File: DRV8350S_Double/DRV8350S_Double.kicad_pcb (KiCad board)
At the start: 4 copper layers, 180.5 x 154.9 mm, 248 parts, among them IC1 MCP1501T-33, J1 USB_OTG, J10 Screw_Terminal_01x01, J11 Screw_Terminal_01x01, J12 Screw_Terminal_01x01, J13 Screw_Terminal_01x01, J14 Screw_Terminal_01x01, J15 Screw_Terminal_01x01, J16 Screw_Terminal_01x01, J17 Screw_Terminal_01x01, J18 Conn_01x08, J2 Conn_02x07_Odd_Even, J3 Conn_01x04, J4 47272-0001, J5 Conn_01x08, J6 Conn_01x08, J7 Conn_01x08, J8 Conn_01x08, J9 47272-0001, Q1 Q_NMOS_GDS, Q10 Q_NMOS_GDS, Q11 Q_NMOS_GDS, Q12 Q_NMOS_GDS, Q2 Q_NMOS_GDS, Q3 Q_NMOS_GDS, Q4 Q_NMOS_GDS, Q5 Q_NMOS_GDS, Q6 Q_NMOS_GDS, Q7 Q_NMOS_GDS, Q8 Q_NMOS_GDS, Q9 Q_NMOS_GDS, SW2 SW_Push, U1 LM5017MR, U10 SN65LVDS31D, U11 LM324DR, U12 LM324DR, U13 ESD122DMXR, U14 SN65LVDS33D, U15 LSF0204PWR, U16 LSF0204PWR, U17 LM324DR, U2 ADUM4160, U3 LM2576HVS-5, U4 LM2576HVS-3.3, U5 ISO1050-CUSTOM-SuperDriver_1.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, U6 STM32H743VITx, U7 DRV8350, U8 DRV8350, U9 SN65LVDS31D, Y1 SIT8008AI-82-33E-22.118400

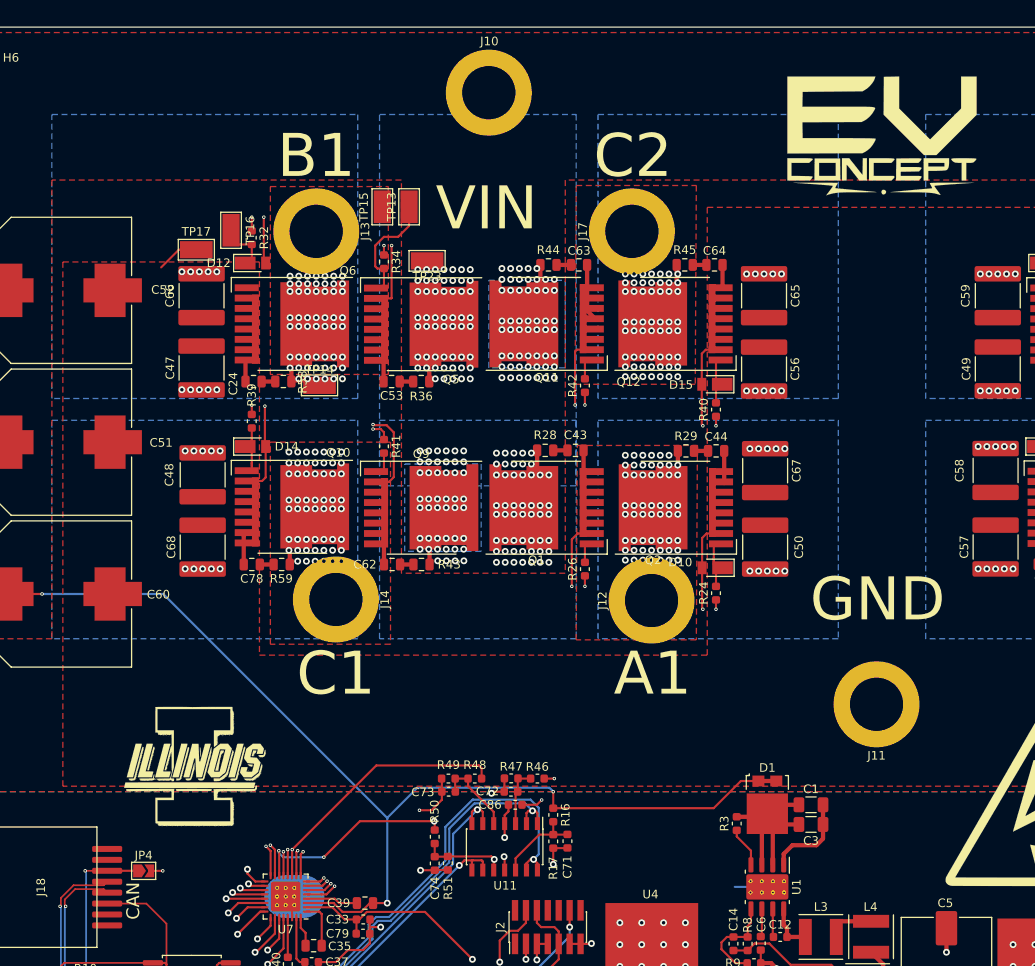
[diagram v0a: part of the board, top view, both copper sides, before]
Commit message: fixed iso_gnd miss
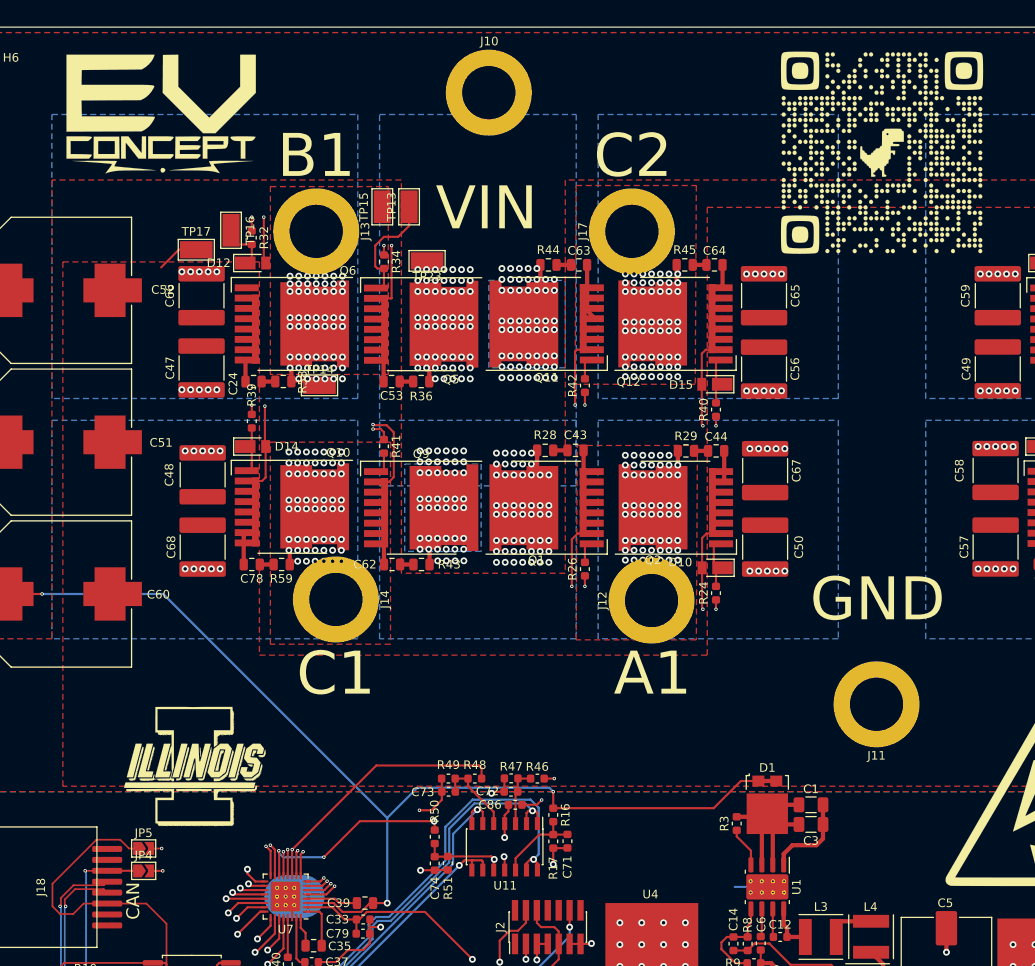
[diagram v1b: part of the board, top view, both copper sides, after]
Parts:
- added JP5: SJ-O, Jumper:SolderJumper-2_P1.3mm_Open_TrianglePad1.0x1.5mm, F.Cu at (56.4, 110.7)
- added NA3: Image, EVCONCEPT:qrcode_github, F.Cu at (142.2, 29.8)
- moved NA2 83.9 mm to (58.4, 25.4)
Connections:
- R41 pad 1: C1 -> GHC1
- U7 pad 13: C1 -> GHC1
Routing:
- net GHC1: track 0.00 -> 61.9 mm, vias 0 -> 3
- net C1: track 167.1 -> 105.2 mm, vias 61 -> 58
- net GND_ISO: track 59.1 -> 81.4 mm
- net GND: track 1005.9 -> 1007.3 mm, vias 116 -> 117

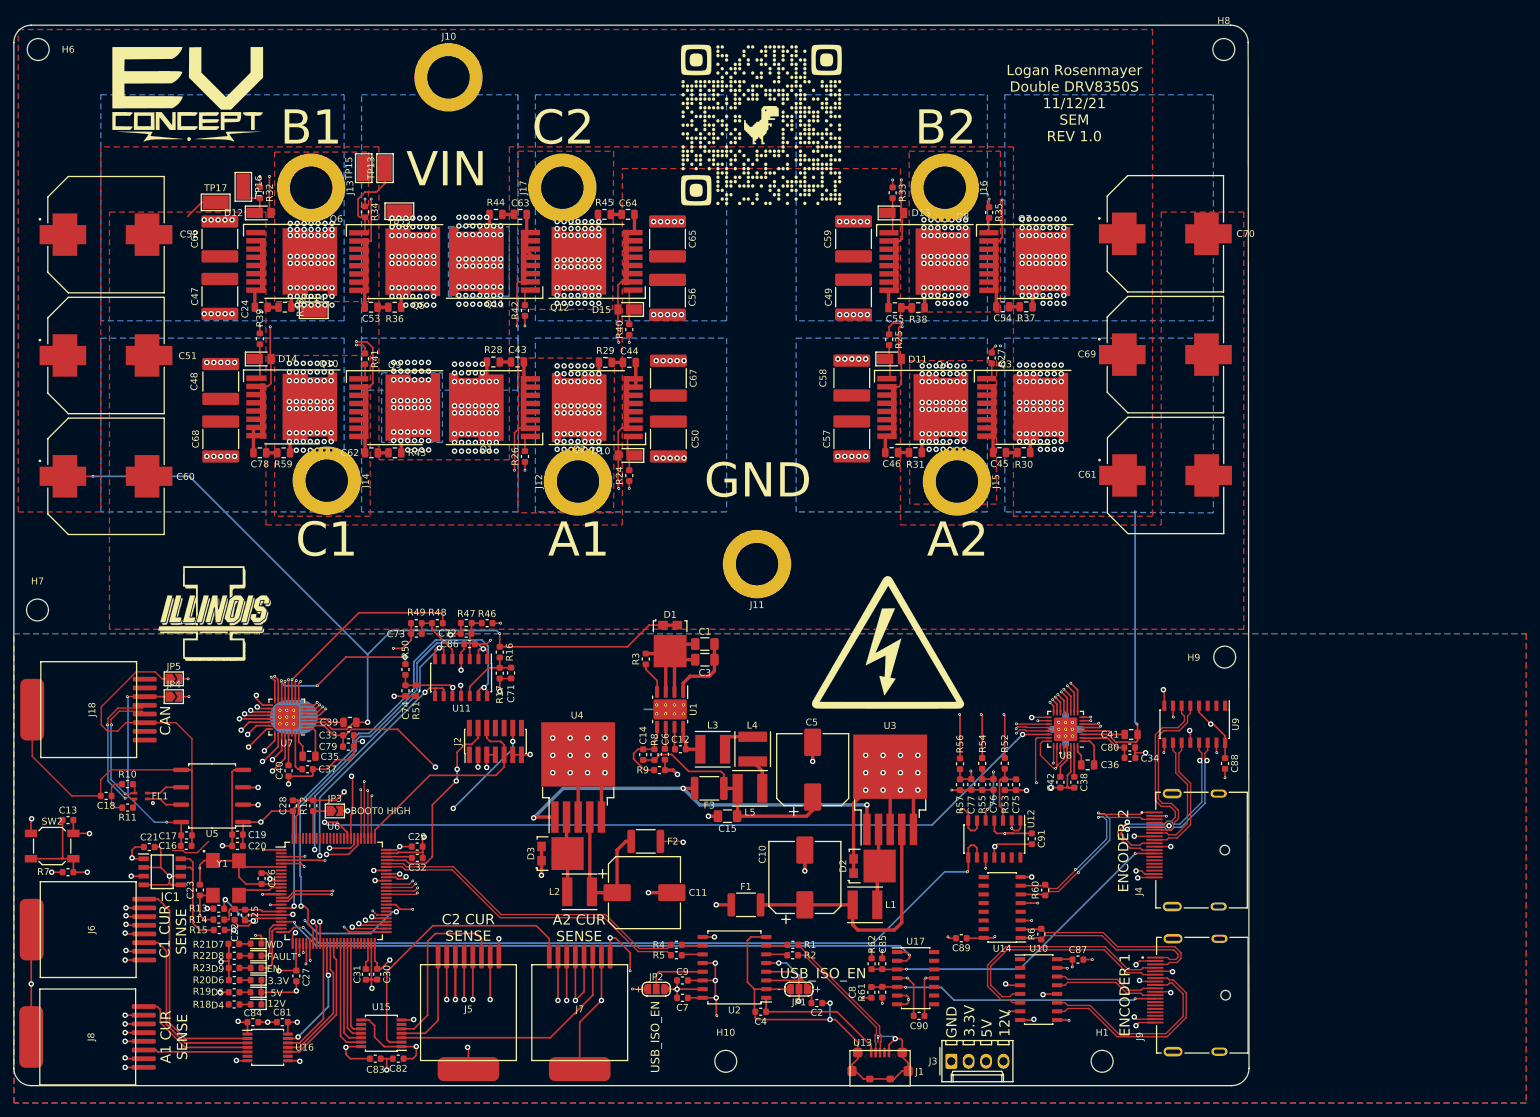
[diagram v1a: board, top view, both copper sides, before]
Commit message: Backing up current design
Fucked up something with STM32 and displayport is dumb
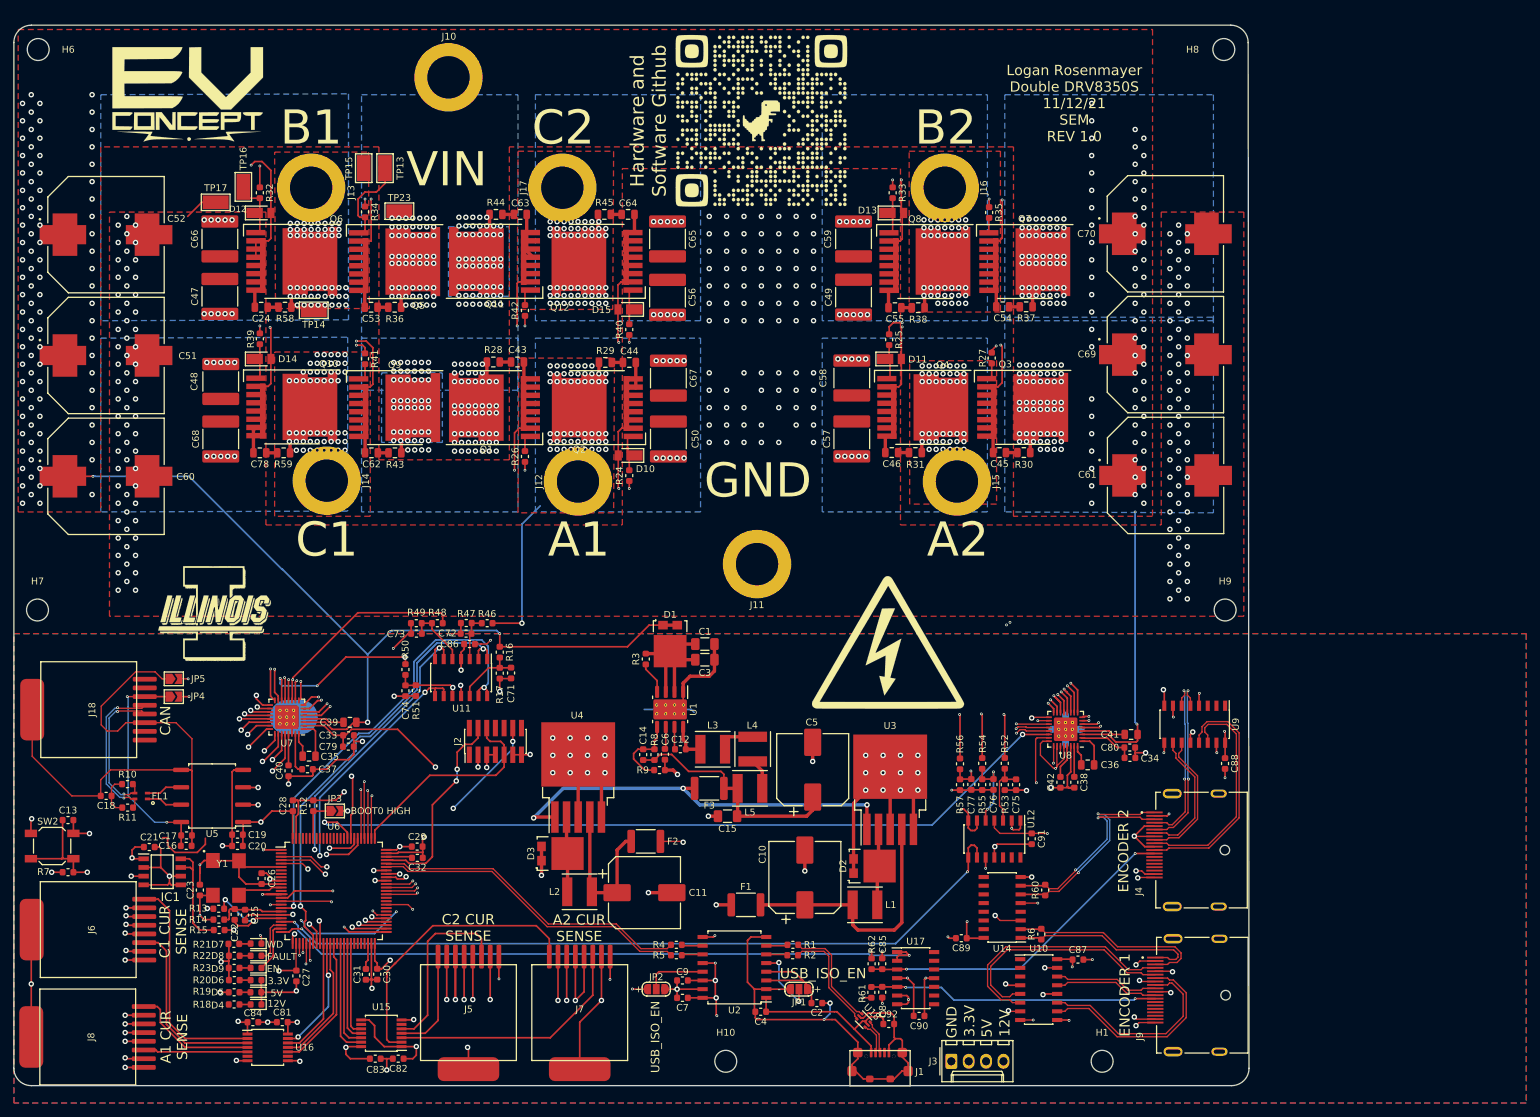
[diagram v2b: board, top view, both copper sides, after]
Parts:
- removed U13: ESD122DMXR, EVCONCEPT:IC_ESD122DMXR
- added C92: 0.1uF, Capacitor_SMD:C_0603_1608Metric, F.Cu at (160.8, 161.2)
- added NA7: Image, EVCONCEPT:qr_code_rick_roll, F.Cu at (142.2, 29.2)
- added U18: USBLC6-2SC6, Package_TO_SOT_SMD:SOT-666, F.Cu at (157.2, 160.7)
- NA3: moved to B.Cu
- moved NA3 128.0 mm to (49.5, 118.1), turned to 180 degrees
- moved H9 6.88 mm to (210.0, 100.7)
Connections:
- net ~Fault1 renamed ~{Fault1}
- net ~Fault2 renamed ~{Fault2}
- J1 pad 2: /UD_Conn_- -> /UD_Conn_preESD_-
- J1 pad 3: /UD_Conn_+ -> /UD_Conn_preESD_+
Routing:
- net GND: track 1007.3 -> 1041.3 mm, vias 117 -> 326
- net GLB1: track 81.6 -> 98.8 mm
- net A2: track 102.8 -> 111.9 mm, vias 58 -> 44
- net +5V: track 74.0 -> 64.9 mm, vias 16 -> 15
- net VBUS1: track 20.4 -> 27.0 mm
- net USBGND: track 65.5 -> 71.5 mm, vias 4 -> 2
- net SPI6_nSS_-: track 30.5 -> 35.7 mm, vias 2 -> 0
- net /UD_Conn_preESD_+: track 0.00 -> 5.07 mm
- net /UD_Conn_preESD_-: track 0.00 -> 4.74 mm
- net GHA2: track 67.3 -> 72.0 mm
- net /UD_Conn_+: track 20.8 -> 16.2 mm
- net SPI4_MISO: track 124.1 -> 119.7 mm
- net SPI6_nSS_+: track 29.5 -> 33.7 mm, vias 2 -> 0
- net Net-(D12-Pad1): track 6.69 -> 10.7 mm
- net SPI6_MOSI: track 161.2 -> 165.0 mm
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- added copper zone on In2.Cu, net GND
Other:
- net class Default removed
- board text added: "Hardware and Software Github"
